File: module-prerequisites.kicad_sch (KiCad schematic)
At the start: 0 parts

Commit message: Work on Prerequisites sheet
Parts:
- added C1, C2: 1µf, symbol Device:C_Small
- added J1: Conn_01x12, symbol Connector_Generic:Conn_01x12
- added R1: 10kΩ, symbol Device:R_Small
- added U1: AP2127K-3.3, Package_TO_SOT_SMD:SOT-23-5, symbol Regulator_Linear:AP2127K-3.3
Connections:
- net 3V3: now also C2.1, U1.5 (VOUT)
- net ENABLE: now also J1.4 (Pin_4), R1.1, U1.3 (EN)
- net SCL: now also J1.8 (Pin_8)
- net SDA: now also J1.9 (Pin_9)
- new net GND: C1.2, C2.2, J1.2 (Pin_2), R1.2, U1.2 (GND)
- new net HOST-3V3: J1.3 (Pin_3)
- new net PICO: J1.10 (Pin_10)
- new net POCI: J1.11 (Pin_11)
- new net SCK: J1.12 (Pin_12)
- new net VIN: C1.1, J1.1 (Pin_1), U1.1 (VIN)
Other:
- note added: "300mA MAXIMUM"
- note added: "DEPRECATED"
- note added: "HOST-3V3 IS AVAILABLE EVEN WHEN MODULE IS DISABLED. USE WITH CAUTION."
- note added: "MODULE CONNECTOR"
- note added: "POWER REGULATION"
- note added: "RESERVED"
- company: (none) -> Fieldkit
- title: (none) -> Module Prerequisites

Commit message: Finished prerequisites. Started component placement.
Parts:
- added C3: .1μf, !magpie:R0603, symbol !magpie:C_Bypass
- added R2, R3: 4.7kΩ, !magpie:R0603, symbol Device:R_Small
- added U2: M24C64-DFMN6TP, Package_SO:SOIC-8_3.9x4.9mm_P1.27mm, symbol Memory_EEPROM:M24C01-FMN
- C1, C2, R1: footprint (none) -> !magpie:R0603
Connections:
- net 3V3: now also C3.1, U2.8 (VCC)
- net GND: now also C3.2, U2.1 (E0), U2.2 (E1), U2.3 (E2), U2.4 (VSS)
- net HOST-3V3: now also R2.2, R3.2
- net SCL: now also R2.1, U2.6 (SCL)
- net SDA: now also R3.1, U2.5 (SDA)
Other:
- note added: "EEPROM"
- note added: "EEPROM DATA IS USED TO IDENTIFY MODULES AND STORE CALIBRATION"
- note added: "HOST POWER IS USED FOR PULLUPS BECAUSE I2C LINES ARE MONITORED TO DETECT MODULE HOT INSERTION EVEN WHEN NOT ENABLED"
- moved on the sheet: C1, C2, J1, R1, U1

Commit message: Board routing complete.
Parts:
- J1: footprint (none) -> !magpie:M20-7810645R
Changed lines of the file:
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@@
     (stroke (width 0) (type default))
   )
-  (wire (pts (xy 142.24 35.56) (xy 152.4 35.56))
+  (wire (pts (xy 142.24 35.56) (xy 157.48 35.56))
     (stroke (width 0) (type default))
   )
@@
     (effects (font (size 1.27 1.27)) (justify right bottom))
   )
-  (label "ENABLE" (at 152.4 35.56 180) (fields_autoplaced)
+  (label "ENABLE" (at 157.48 35.56 180) (fields_autoplaced)
     (effects (font (size 1.27 1.27)) (justify right bottom))
   )
@@
     (effects (font (size 1.27 1.27)) (justify left))
   )
-  (hierarchical_label "ENABLE" (shape output) (at 152.4 35.56 0) (fields_autoplaced)
+  (hierarchical_label "ENABLE" (shape output) (at 157.48 35.56 0) (fields_autoplaced)
     (effects (font (size 1.27 1.27)) (justify left))
   )
@@
       (effects (font (size 1.27 1.27)) hide)
     )
-    (property "Footprint" "" (at 137.16 40.64 0)
-      (effects (font (size 1.27 1.27)) hide)
-    )
+    (property "Footprint" "!magpie:M20-7810645R" (at 137.16 40.64 0)
+      (effects (font (size 1.27 1.27)) hide)
+    )

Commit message: Cleaning up file system.
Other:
- note added: "HOST-3V3 IS AVAILABLE EVEN WHEN MODULE IS DISABLED USE WITH CAUTION"
- note removed: "HOST-3V3 IS AVAILABLE EVEN WHEN MODULE IS DISABLED. USE WITH CAUTION."
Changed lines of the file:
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@@
     (effects (font (size 1.27 1.27)) (justify left bottom))
   )
-  (text "HOST-3V3 IS AVAILABLE EVEN WHEN MODULE IS DISABLED.\nUSE WITH CAUTION."
+  (text "HOST-3V3 IS AVAILABLE EVEN WHEN MODULE IS DISABLED\nUSE WITH CAUTION"
     (at 170.18 66.04 0)
     (effects (font (size 1.27 1.27)) (justify right bottom))

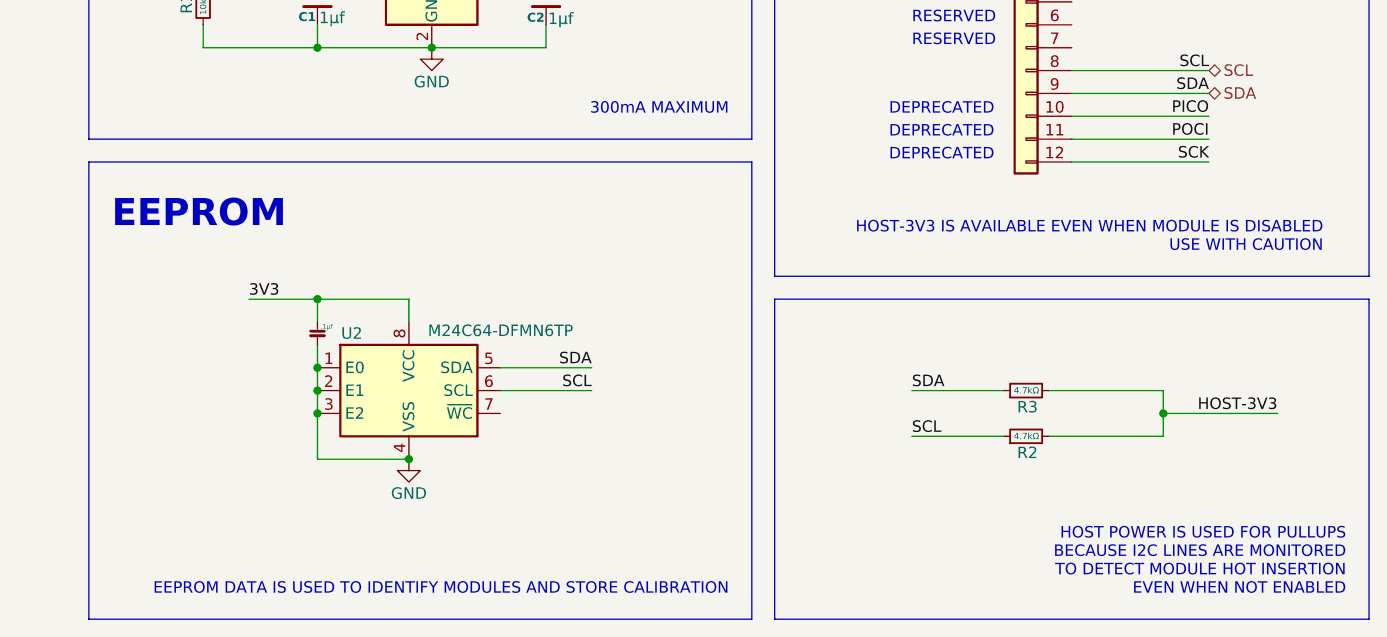
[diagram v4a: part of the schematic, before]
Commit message: Small aesthetic channges, and KiCad version update.
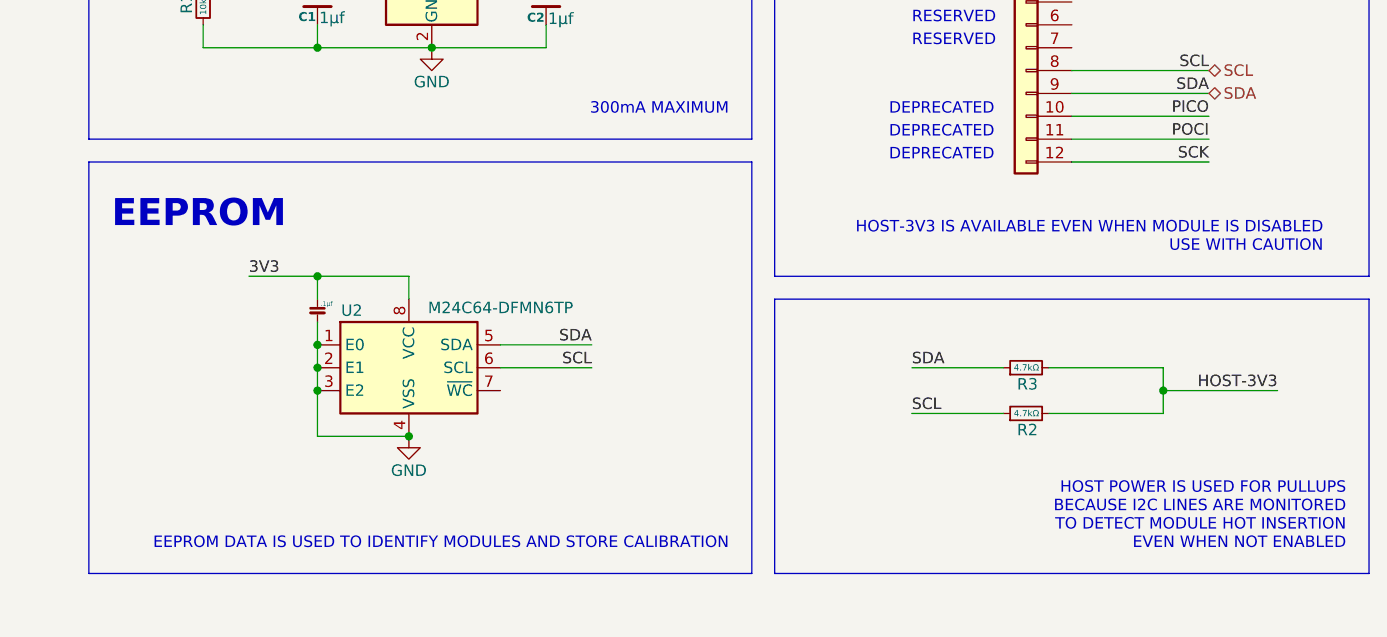
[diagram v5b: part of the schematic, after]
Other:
- company: Fieldkit -> (none)
- title: Module Prerequisites -> Fieldkit Module Prerequisittes
- moved on the sheet: R2, R3, U2
